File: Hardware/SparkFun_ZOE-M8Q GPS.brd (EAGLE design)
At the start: 25.4 x 25.4 mm, 62 parts, among them J4 U.FL, U1 UBLOX_ZOE_M8-0-10, Y1 32.768kHz

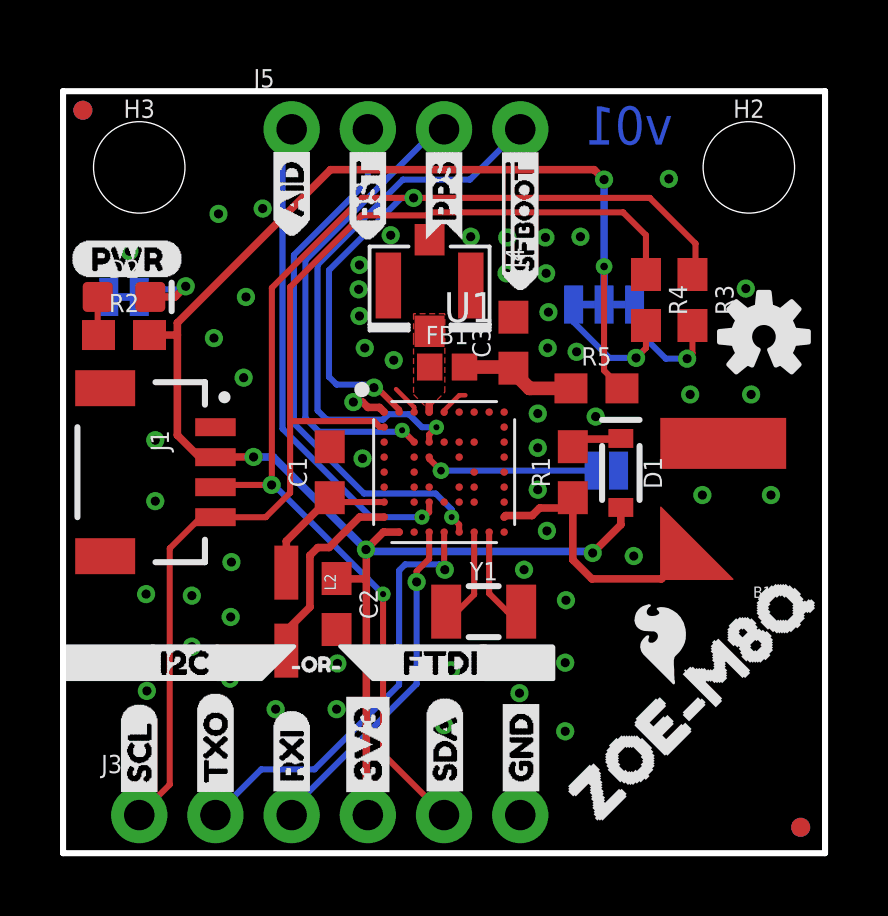
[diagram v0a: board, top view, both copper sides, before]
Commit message: Updates schematic frame to letter size, updates parts (see description)
* Battery part updated - replaces 100 Ohm series reistor with 3.3K
* IC part updated - better pin names on symbol
* Inductor part updated with better pads
* 8 Pin connector added - moves SDA and SCL to their own through hole
* Adds and fixes silk around design
* Adds thermals to ground pour
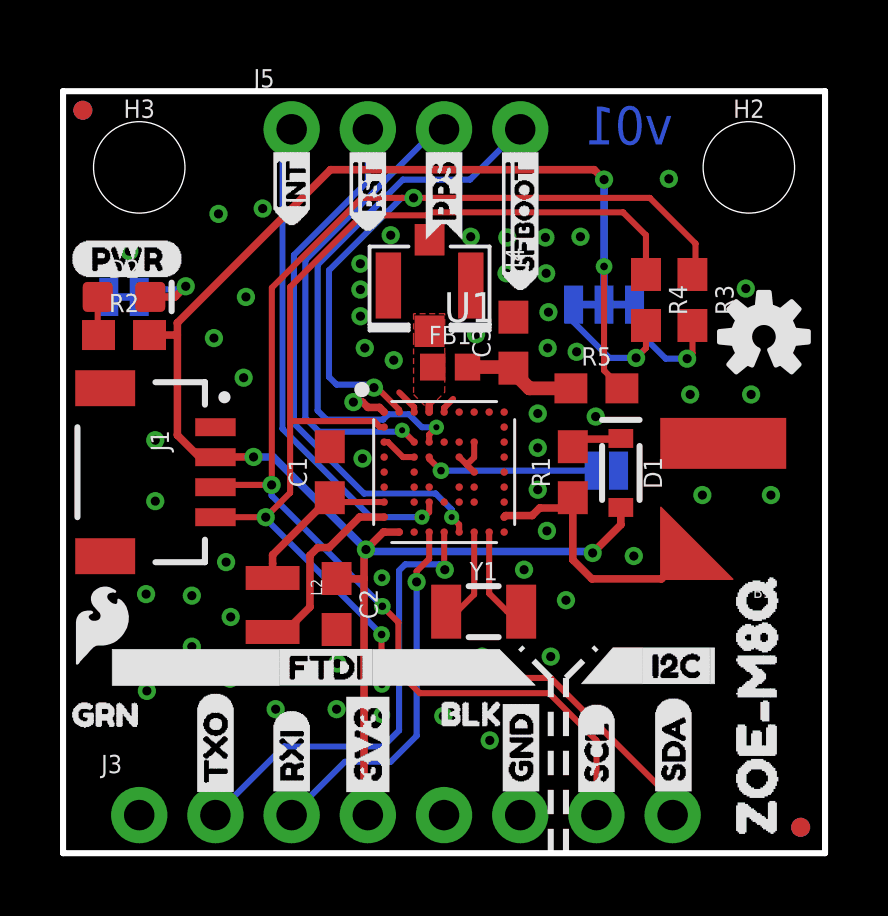
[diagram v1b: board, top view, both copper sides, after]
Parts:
- removed U$22: (no value), RESET:RST0
- added U$31: (no value), GRN:GRN0
- added U$32: (no value), Labels:I_SUPER2_C-()-04
- FRAME1: value FRAME-LEDGER -> FRAME-LETTER
- J3: device SparkFun-Connectors:1X06_NO_SILK -> SparkFun-Connectors:1X08_NO_SILK
- L2: value 2.2UH_SHIELDED_INDUCTOR -> 2.2uH; device SparkFun-Coils:UNIQUE_0806_NDUC -> SparkFun-Coils:0806
- R1: value 100 -> 3.3k
- U$11: device AID:AID0 -> INT:#INT0
- U$12: device RESET:RST0 -> RESET:#RST0
- U$18: device I2C_PU:I2C_PU0 -> INT:#INT0
- U$20: device ZOE-M8Q:ZOE#M8Q0 -> BLK:BLK0
- U$21: device AID:AID0 -> RESET:#RST0
- U$28: device I2C_MINOR:I2C0 -> FTDI_SMALL:FTDI0
- U$29: device FTDI_SMALL:FTDI0 -> I2C_MINOR:I2C0
- U$30: device OR:#OR#0 -> ZOE-M8Q_SMALL:ZOE#M8Q0
- moved FRAME1 24.8 mm to (15.7, -21.1)
- moved LOGO3 18.7 mm to (1.29, 7.61), turned to 0 degrees
- moved U$30 17.3 mm to (23.1, -0.51), turned to 90 degrees
- moved U$3 15.2 mm to (17.8, 1.68)
- moved U$8 15.2 mm to (17.8, 1.68)
- moved U$18 13.5 mm to (7.59, 20.7), turned to 90 degrees
- moved U$29 8.28 mm to (18.9, 6.25)
- moved U$2 7.62 mm to (20.3, 1.70)
- moved U$5 7.62 mm to (20.3, 1.68)
- moved U$20 6.01 mm to (11.9, 4.64), turned to 0 degrees
- moved U$28 4.30 mm to (6.83, 6.20)
- moved U$21 2.54 mm to (10.2, 20.6), flipped to the bottom
- moved L2 0.49 mm to (6.99, 7.87)
- moved U$11 0.20 mm to (7.62, 20.7), flipped to the top
- moved U$12 0.20 mm to (10.2, 20.6), flipped to the top
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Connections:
- net INT renamed !INT
- net SCL/CLK: now also J3.7; no longer J3.1
- net SDA/CS: now also J3.8; no longer J3.5
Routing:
- net SCL/CLK: track 38.7 -> 44.5 mm, vias 0 -> 2
- net SDA/CS: track 49.2 -> 54.9 mm
- net GND: track 3.18 -> 5.36 mm, vias 54 -> 57
- net TXO/MISO: track 14.7 -> 15.6 mm
- net RXI/MOSI: track 11.3 -> 12.2 mm

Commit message: Moves Creative License text to the correct place.
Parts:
- moved FRAME1 25.1 mm to (-7.87, -12.7)
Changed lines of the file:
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@@
 <layer number="115" name="ReferenceISLANDS" color="7" fill="1" visible="no" active="no"/>
 <layer number="116" name="Patch_BOT" color="9" fill="4" visible="no" active="no"/>
-<layer number="117" name="PM_Ref" color="26" fill="1" visible="yes" active="yes"/>
+<layer number="117" name="PM_Ref" color="26" fill="1" visible="no" active="yes"/>
 <layer number="118" name="Rect_Pads" color="7" fill="1" visible="no" active="no"/>
-<layer number="119" name="PF_Ref" color="31" fill="1" visible="yes" active="yes"/>
-<layer number="120" name="WFL_Ref" color="25" fill="1" visible="yes" active="yes"/>
+<layer number="119" name="PF_Ref" color="31" fill="1" visible="no" active="yes"/>
+<layer number="120" name="WFL_Ref" color="25" fill="1" visible="no" active="yes"/>
 <layer number="121" name="_tsilk" color="7" fill="1" visible="no" active="no"/>
 <layer number="122" name="_bsilk" color="7" fill="1" visible="no" active="no"/>
@@
 <attribute name="VALUE" x="8.3566" y="8.3058" size="0.6096" layer="27" font="vector" ratio="20" rot="R270" align="top-center"/>
 </element>
-<element name="FRAME1" library="SparkFun-Aesthetics" package="CREATIVE_COMMONS" value="FRAME-LETTER" x="15.748" y="-21.082" smashed="yes">
-<attribute name="DESIGNER" value="" x="15.748" y="-21.082" size="1.778" layer="27" display="off"/>
-<attribute name="REV" value="" x="15.748" y="-21.082" size="1.778" layer="27" display="off"/>
+<element name="FRAME1" library="SparkFun-Aesthetics" package="CREATIVE_COMMONS" value="FRAME-LETTER" x="-7.874" y="-12.7" smashed="yes">
+<attribute name="DESIGNER" value="" x="-7.874" y="-12.7" size="1.778" layer="27" display="off"/>
+<attribute name="REV" value="" x="-7.874" y="-12.7" size="1.778" layer="27" display="off"/>
 </element>
 <element name="U$28" library="FTDI_SMALL" package="FTDI0" value="" x="6.8326" y="6.1976" smashed="yes"/>

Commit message: Adds production files and signature scorpion silk to underside of board.
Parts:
- added U$22: (no value), SCORP_SMALL:SILHOUETTE#OF#A#SCORPION#JPG
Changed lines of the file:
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@@
 <layer number="115" name="ReferenceISLANDS" color="7" fill="1" visible="no" active="no"/>
 <layer number="116" name="Patch_BOT" color="9" fill="4" visible="no" active="no"/>
-<layer number="117" name="PM_Ref" color="26" fill="1" visible="no" active="yes"/>
+<layer number="117" name="PM_Ref" color="26" fill="1" visible="yes" active="yes"/>
 <layer number="118" name="Rect_Pads" color="7" fill="1" visible="no" active="no"/>
-<layer number="119" name="PF_Ref" color="31" fill="1" visible="no" active="yes"/>
-<layer number="120" name="WFL_Ref" color="25" fill="1" visible="no" active="yes"/>
+<layer number="119" name="PF_Ref" color="31" fill="1" visible="yes" active="yes"/>
+<layer number="120" name="WFL_Ref" color="25" fill="1" visible="yes" active="yes"/>
 <layer number="121" name="_tsilk" color="7" fill="1" visible="no" active="no"/>
 <layer number="122" name="_bsilk" color="7" fill="1" visible="no" active="no"/>
@@
 <element name="U$12" library="RESET" package="#RST0" value="" x="10.16" y="20.574" smashed="yes" rot="R90"/>
 <element name="U$21" library="RESET" package="#RST0" value="" x="10.16" y="20.574" smashed="yes" rot="MR90"/>
+<element name="U$22" library="SCORP_SMALL" package="SILHOUETTE#OF#A#SCORPION#JPG" value="" x="19.812" y="9.398" smashed="yes" rot="MR0"/>
 </elements>
 <signals>

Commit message: Removes some silk, changes version number, removes prototype gerber files
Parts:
- removed U$22: (no value), SCORP_SMALL:SILHOUETTE#OF#A#SCORPION#JPG
- moved LOGO3 11.4 mm to (7.39, 17.3)
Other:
- board text added: "v10"
- board text removed: "v01"
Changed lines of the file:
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@@
 <layer number="115" name="ReferenceISLANDS" color="7" fill="1" visible="no" active="no"/>
 <layer number="116" name="Patch_BOT" color="9" fill="4" visible="no" active="no"/>
-<layer number="117" name="PM_Ref" color="26" fill="1" visible="yes" active="yes"/>
+<layer number="117" name="PM_Ref" color="26" fill="1" visible="no" active="yes"/>
 <layer number="118" name="Rect_Pads" color="7" fill="1" visible="no" active="no"/>
-<layer number="119" name="PF_Ref" color="31" fill="1" visible="yes" active="yes"/>
-<layer number="120" name="WFL_Ref" color="25" fill="1" visible="yes" active="yes"/>
+<layer number="119" name="PF_Ref" color="31" fill="1" visible="no" active="yes"/>
+<layer number="120" name="WFL_Ref" color="25" fill="1" visible="no" active="yes"/>
 <layer number="121" name="_tsilk" color="7" fill="1" visible="no" active="no"/>
 <layer number="122" name="_bsilk" color="7" fill="1" visible="no" active="no"/>
@@
 <wire x1="0" y1="25.4" x2="0" y2="0" width="0.2032" layer="20"/>
 <text x="19.05" y="-12.7" size="1.778" layer="51" font="vector" ratio="15">Elias Santistevan</text>
-<text x="20.32" y="23.622" size="1.27" layer="16" font="vector" ratio="15" rot="MR0">v01</text>
+<text x="20.32" y="23.622" size="1.27" layer="16" font="vector" ratio="15" rot="MR0">v10</text>
 <dimension x1="25.4" y1="25.4" x2="25.4" y2="0" x3="31.75" y3="12.7" textsize="1.27" textratio="15" layer="47" dtype="vertical" unit="inch"/>
 <polygon width="0.127" layer="22">
@@
 <element name="LOGO2" library="SparkFun-Aesthetics" package="OSHW-LOGO-S" value="OSHW-LOGOS" x="23.362921875" y="17.213578125" smashed="yes"/>
 <element name="U$16" library="ZOE-M8Q" package="ZOE#M8Q0" value="" x="12.7508" y="12.6238" smashed="yes" rot="MR0"/>
-<element name="LOGO3" library="SparkFun-Aesthetics" package="SFE_LOGO_FLAME_.1" value="SFE_LOGO_FLAME.1_INCH" x="1.290315625" y="7.609840625" smashed="yes"/>
+<element name="LOGO3" library="SparkFun-Aesthetics" package="SFE_LOGO_FLAME_.1" value="SFE_LOGO_FLAME.1_INCH" x="7.386315625" y="17.261840625" smashed="yes"/>
 <element name="U$17" library="SPI_JUMPER" package="SPI0" value="" x="19.52498125" y="11.04391875" smashed="yes" rot="MR0"/>
 <element name="D2" library="SparkFun-LED" package="LED-0603" value="RED" x="2.032" y="18.542" smashed="yes">
@@
 <element name="U$12" library="RESET" package="#RST0" value="" x="10.16" y="20.574" smashed="yes" rot="R90"/>
 <element name="U$21" library="RESET" package="#RST0" value="" x="10.16" y="20.574" smashed="yes" rot="MR90"/>
-<element name="U$22" library="SCORP_SMALL" package="SILHOUETTE#OF#A#SCORPION#JPG" value="" x="19.812" y="9.398" smashed="yes" rot="MR0"/>
 </elements>
 <signals>

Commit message: Adds silk to battery terminals, adds initial mAH text to battery section in schematic.
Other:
- board text added: "+"
- board text added: "-"
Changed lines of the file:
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@@
 <layer number="115" name="ReferenceISLANDS" color="7" fill="1" visible="no" active="no"/>
 <layer number="116" name="Patch_BOT" color="9" fill="4" visible="no" active="no"/>
-<layer number="117" name="PM_Ref" color="26" fill="1" visible="no" active="yes"/>
+<layer number="117" name="PM_Ref" color="26" fill="1" visible="yes" active="yes"/>
 <layer number="118" name="Rect_Pads" color="7" fill="1" visible="no" active="no"/>
-<layer number="119" name="PF_Ref" color="31" fill="1" visible="no" active="yes"/>
-<layer number="120" name="WFL_Ref" color="25" fill="1" visible="no" active="yes"/>
+<layer number="119" name="PF_Ref" color="31" fill="1" visible="yes" active="yes"/>
+<layer number="120" name="WFL_Ref" color="25" fill="1" visible="yes" active="yes"/>
 <layer number="121" name="_tsilk" color="7" fill="1" visible="no" active="no"/>
 <layer number="122" name="_bsilk" color="7" fill="1" visible="no" active="no"/>
@@
 <vertex x="21.572221875" y="6.8427625"/>
 </polygon>
+<text x="21.2852" y="14.2494" size="1.778" layer="21" font="vector" ratio="15">-</text>
+<text x="19.8374" y="7.6454" size="1.778" layer="21" font="vector" ratio="15">+</text>
 </plain>
 <attributes>

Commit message: Adds no connect silk, fixes net labels that have active low pins
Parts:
- added U$22, U$33, U$34, U$35: (no value), NC:NC0
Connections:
- net RESET renamed !RESET
- net SAFEBOOT renamed !SAFEBOOT
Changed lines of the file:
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@@
 <wire x1="0" y1="25.4" x2="0" y2="0" width="0.2032" layer="20"/>
 <text x="19.05" y="-12.7" size="1.778" layer="51" font="vector" ratio="15">Elias Santistevan</text>
-<text x="20.32" y="23.622" size="1.27" layer="16" font="vector" ratio="15" rot="MR0">v10</text>
+<text x="24.638" y="21.082" size="1.27" layer="16" font="vector" ratio="15" rot="SMR270">v10</text>
 <dimension x1="25.4" y1="25.4" x2="25.4" y2="0" x3="31.75" y3="12.7" textsize="1.27" textratio="15" layer="47" dtype="vertical" unit="inch"/>
 <polygon width="0.127" layer="22">
@@
 <element name="U$12" library="RESET" package="#RST0" value="" x="10.16" y="20.574" smashed="yes" rot="R90"/>
 <element name="U$21" library="RESET" package="#RST0" value="" x="10.16" y="20.574" smashed="yes" rot="MR90"/>
+<element name="U$22" library="NC" package="NC0" value="" x="12.7" y="1.778" smashed="yes" rot="R90"/>
+<element name="U$33" library="NC" package="NC0" value="" x="2.54" y="1.778" smashed="yes" rot="R90"/>
+<element name="U$34" library="NC" package="NC0" value="" x="12.7" y="1.778" smashed="yes" rot="MR90"/>
+<element name="U$35" library="NC" package="NC0" value="" x="2.54" y="1.778" smashed="yes" rot="MR90"/>
 </elements>
 <signals>
@@
 <wire x1="12.7" y1="24.13" x2="12.446" y2="24.13" width="0.2032" layer="16"/>
 </signal>
-<signal name="SAFEBOOT">
+<signal name="!SAFEBOOT">
 <contactref element="U1" pad="34"/>
 <via x="12.446" y="14.1986" extent="1-16" drill="0.2032"/>
@@
 <wire x1="8.4836" y1="19.6088" x2="11.3284" y2="22.4536" width="0.2032" layer="16"/>
 </signal>
-<signal name="RESET">
+<signal name="!RESET">
 <contactref element="U1" pad="20"/>
 <via x="12.954" y="11.2014" extent="1-16" drill="0.2032"/>

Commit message: Adds special ordering instructions and qwiic silk
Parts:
- added LOGO4: SPECIAL_INSTRUCTIONS-ORDERING, SparkFun-Aesthetics:ORDERING_INSTRUCTIONS
- added U$36: (no value), Labels:QWIIC_COPYRIGHT_SMALL
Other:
- board text added: "0.8mm Board Thickness"
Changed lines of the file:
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@@
 <text x="21.2852" y="14.2494" size="1.778" layer="21" font="vector" ratio="15">-</text>
 <text x="19.8374" y="7.6454" size="1.778" layer="21" font="vector" ratio="15">+</text>
+<text x="-25.4" y="-31.496" size="1.778" layer="51" font="vector" ratio="15">0.8mm Board Thickness</text>
 </plain>
 <attributes>
@@
 <element name="U$34" library="NC" package="NC0" value="" x="12.7" y="1.778" smashed="yes" rot="MR90"/>
 <element name="U$35" library="NC" package="NC0" value="" x="2.54" y="1.778" smashed="yes" rot="MR90"/>
+<element name="U$36" library="Labels" package="QWIIC_COPYRIGHT_SMALL" value="" x="6.096" y="10.414" smashed="yes" rot="MR0"/>
+<element name="LOGO4" library="SparkFun-Aesthetics" package="ORDERING_INSTRUCTIONS" value="SPECIAL_INSTRUCTIONS-ORDERING" x="-27.94" y="-18.288" smashed="yes"/>
 </elements>
 <signals>

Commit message: Updates schematic
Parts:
- U1: value UBLOX_ZOE_M8-0-10 -> U-BLOX_ZOE_M8Q-0-10
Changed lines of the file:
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@@
 <?xml version="1.0" encoding="utf-8"?>
 <!DOCTYPE eagle SYSTEM "eagle.dtd">
-<eagle version="9.2.1">
+<eagle version="9.6.2">
 <drawing>
 <settings>
@@
 <setting verticaltext="up"/>
 </settings>
-<grid distance="0.01" unitdist="inch" unit="inch" style="lines" multiple="1" display="yes" altdistance="0.001" altunitdist="inch" altunit="inch"/>
+<grid distance="0.05" unitdist="inch" unit="inch" style="dots" multiple="1" display="yes" altdistance="0.005" altunitdist="inch" altunit="inch"/>
 <layers>
 <layer number="1" name="Top" color="4" fill="1" visible="yes" active="yes"/>
 <layer number="2" name="Route2" color="16" fill="1" visible="no" active="no"/>
 <layer number="15" name="Route15" color="23" fill="1" visible="no" active="no"/>
-<layer number="16" name="Bottom" color="31" fill="1" visible="yes" active="yes"/>
-<layer number="17" name="Pads" color="30" fill="1" visible="yes" active="yes"/>
+<layer number="16" name="Bottom" color="3" fill="1" visible="yes" active="yes"/>
+<layer number="17" name="Pads" color="26" fill="1" visible="yes" active="yes"/>
 <layer number="18" name="Vias" color="2" fill="1" visible="yes" active="yes"/>
 <layer number="19" name="Unrouted" color="6" fill="1" visible="yes" active="yes"/>
@@
 </autorouter>
 <elements>
-<element name="U1" library="SparkFun-GPS" package="UBLOX_ZOE_M8-0-10" value="UBLOX_ZOE_M8-0-10" x="12.7" y="12.7" smashed="yes">
+<element name="U1" library="SparkFun-GPS" package="UBLOX_ZOE_M8-0-10" value="U-BLOX_ZOE_M8Q-0-10" x="12.7" y="12.7" smashed="yes">
 <attribute name="NAME" x="12.7" y="17.7" size="1" layer="25"/>
 <attribute name="PROD_ID" value="IC-14251" x="12.7" y="12.7" size="1.778" layer="27" font="vector" ratio="15" display="off"/>
